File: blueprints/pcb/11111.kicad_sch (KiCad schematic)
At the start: 128 parts, among them J1 TRRS_MJ-4PP-9, J2 TRRS_MJ-4PP-9, SW1 SW_Push, SW10 SW_Push, SW11 SW_Push, SW12 SW_Push, SW13 SW_Push, SW14 SW_Push, SW15 SW_Push, SW16 SW_Push, SW17 SW_Push, SW18 SW_Push, SW19 SW_Push, SW2 SW_Push, SW20 SW_Push, SW21 SW_Push, SW22 SW_Push, SW23 SW_Push, SW24 SW_Push, SW25 SW_Push, SW26 SW_Push, SW27 SW_Push, SW28 SW_Push, SW29 SW_Push, SW3 SW_Push, SW30 SW_Push, SW31 SW_Push, SW32 SW_Push, SW33 SW_Push, SW34 SW_Push, SW35 SW_Push, SW36 SW_Push, SW37 SW_Push, SW38 SW_Push, SW39 SW_Push, SW4 SW_Push, SW40 SW_Push, SW41 SW_Push, SW42 SW_Push, SW43 SW_Push, SW44 SW_Push, SW45 SW_Push, SW46 SW_Push, SW47 SW_Push, SW48 SW_Push, SW49 SW_Push, SW5 SW_Push, SW50 SW_Push, SW51 SW_Push, SW52 SW_Push, SW53 SW_Push, SW54 SW_Push, SW55 SW_Push, SW56 SW_Push, SW57 SW_Push, SW58 SW_Push, SW59 SW_Push, SW6 SW_Push, SW60 SW_Push, SW61 SW_Push, SW62 SW_Push, SW7 SW_Push, SW8 SW_Push, SW9 SW_Push, U1 Pico, U2 Pico

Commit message: オモテウラを間違えていたので修正
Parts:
- D1, D10, D11, D12, D13, D14, D15, D16, D17, D18, D19, D2, D20, D21, D22, D23, D24, D25, D26, D27, D28, D29, D3, D30, D31, D32, D33, D34, D35, D36, D37, D38, D39, D4, D40, D41, D42, D43, D44, D45, D46, D47, D48, D49, D5, D50, D51, D52, D53, D54, D55, D56, D57, D58, D59, D6, D60, D61, D62, D7, D8, D9: footprint Diode_SMD:D_SOD-123 -> Salicylic-acid3_kbd_Parts:Diode_SMD
- SW1, SW10, SW11, SW12, SW13, SW14, SW15, SW16, SW17, SW18, SW19, SW2, SW20, SW21, SW22, SW23, SW24, SW25, SW26, SW27, SW28, SW29, SW3, SW30, SW31, SW32, SW33, SW34, SW35, SW36, SW37, SW38, SW39, SW4, SW40, SW41, SW42, SW43, SW44, SW45, SW46, SW47, SW48, SW49, SW5, SW50, SW51, SW52, SW53, SW54, SW55, SW56, SW57, SW58, SW59, SW6, SW60, SW61, SW62, SW7, SW8, SW9: footprint Button_Switch_Keyboard:SW_Cherry_MX_1.00u_PCB -> Salicylic-acid3_kbd_SW:CherryMX_Solder_1u

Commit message: update PCB
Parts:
- removed U1, U2: Pico, Raspberry-pi-pico:RPi_Pico_SMD_TH, symbol raspberry_pi_pico:Pico
- added R1, R2: 5.1k, Resistor_THT:R_Axial_DIN0204_L3.6mm_D1.6mm_P5.08mm_Vertical, symbol Device:R_Small
- added U1, U2: Pico, Raspberry-pi-pico:RPi_Pico_SMD_TH, symbol raspberry-pi-pico:Pico
- added U3: ~, keyboard_parts:USB_type-C_dip_module_AE-USB2.0-TYPE-C, symbol usb_type-c_dip_connector:USB_type-C_DIP_connector
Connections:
- net Col0: now also U1.29 (GPIO22)
- net Col1: now also U1.27 (GPIO21)
- net Col10: now also U2.25 (GPIO19)
- net Col11: now also U2.24 (GPIO18)
- net Col12: now also U2.22 (GPIO17)
- net Col13: now also U2.21 (GPIO16)
- net Col2: now also U1.26 (GPIO20)
- net Col3: now also U1.25 (GPIO19)
- net Col4: now also U1.24 (GPIO18)
- net Col5: now also U1.22 (GPIO17)
- net Col6: now also U1.21 (GPIO16)
- net Col7: now also U2.29 (GPIO22)
- net Col8: now also U2.27 (GPIO21)
- net Col9: now also U2.26 (GPIO20)
- net DataLeft: now also U1.1 (GPIO0)
- net DataRight: now also U2.1 (GPIO0)
- net GND: now also R1.2, R2.2, U1.13 (GND), U1.18 (GND), U1.23 (GND), U1.28 (GND), U1.3 (GND), U1.38 (GND), U1.8 (GND), U3.4 (GND)
- net GNDA: now also U2.13 (GND), U2.18 (GND), U2.23 (GND), U2.28 (GND), U2.3 (GND), U2.31 (GPIO26_ADC0), U2.38 (GND), U2.8 (GND)
- net Row0: now also U1.15 (GPIO11)
- net Row1: now also U1.16 (GPIO12)
- net Row2: now also U1.17 (GPIO13)
- net Row3: now also U1.19 (GPIO14)
- net Row4: now also U1.20 (GPIO15)
- net Row5: now also U2.15 (GPIO11)
- net Row6: now also U2.16 (GPIO12)
- net Row7: now also U2.17 (GPIO13)
- net Row8: now also U2.19 (GPIO14)
- net Row9: now also U2.20 (GPIO15)
- net VCC: now also U1.31 (GPIO26_ADC0), U1.39 (VSYS)
- net VDD: now also U2.39 (VSYS)
- new net CC1: R1.1, U3.5 (CC1)
- new net CC2: R2.1, U3.6 (CC2)
- new net DM: U3.2 (D-)
- new net DP: U3.3 (D+)
- no-connect marks 38 -> 45

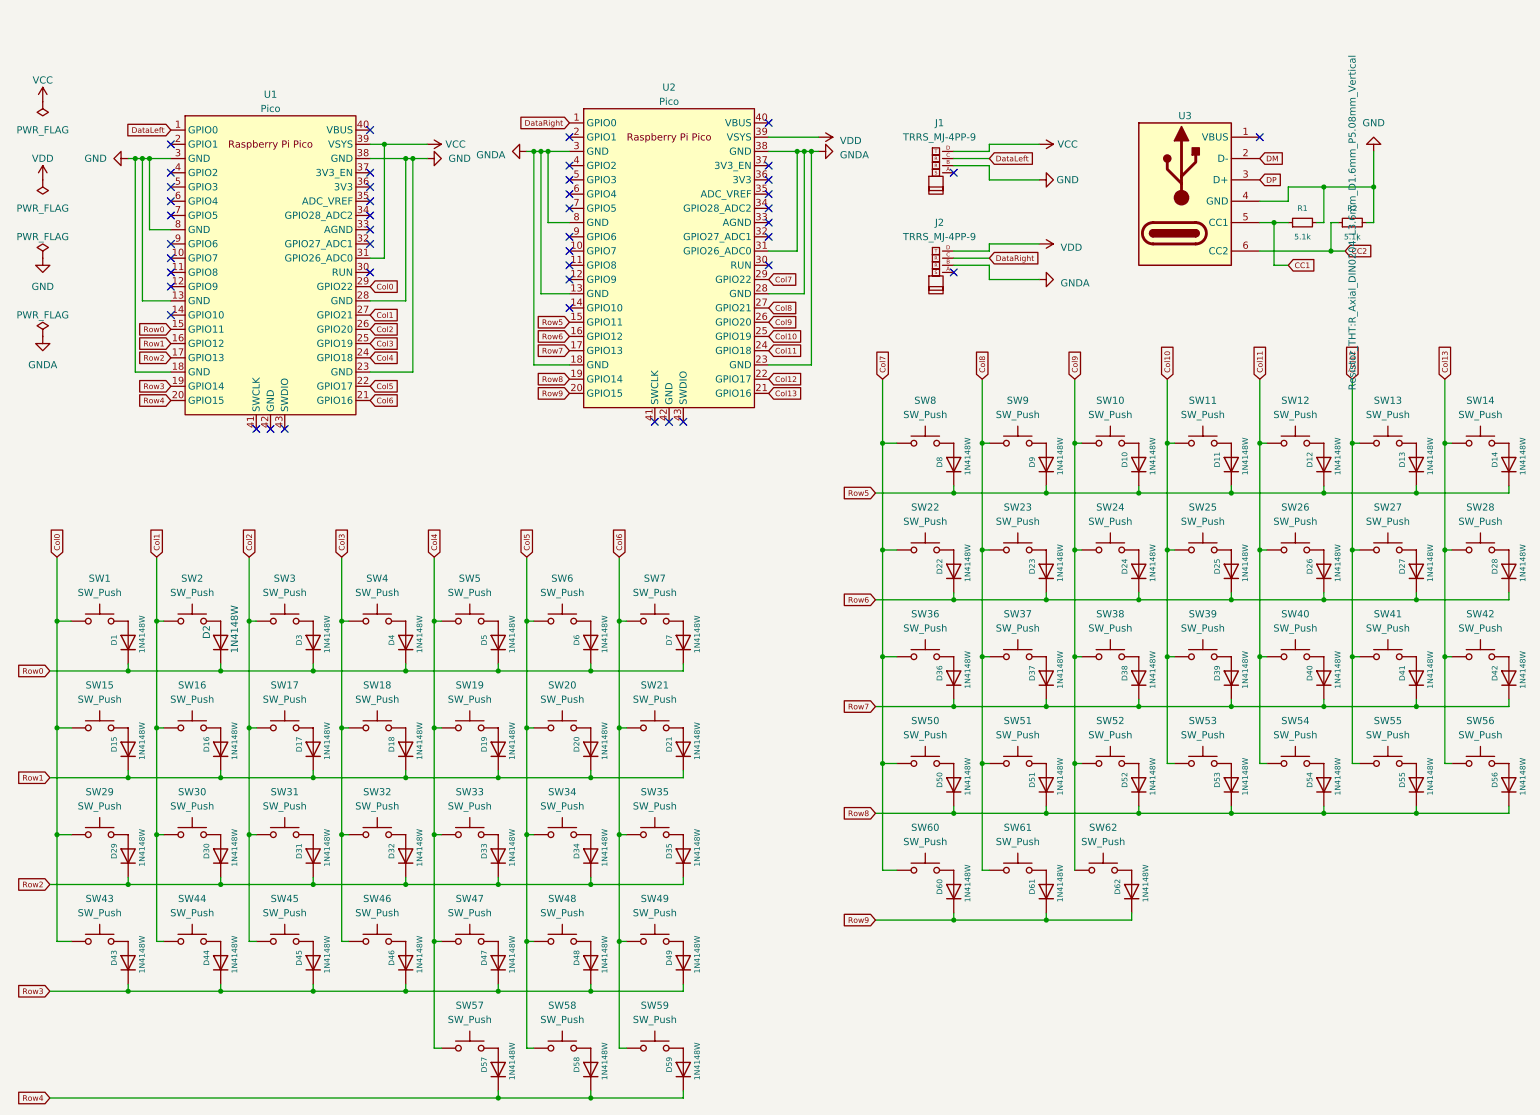
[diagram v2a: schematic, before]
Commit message: add 2 switches
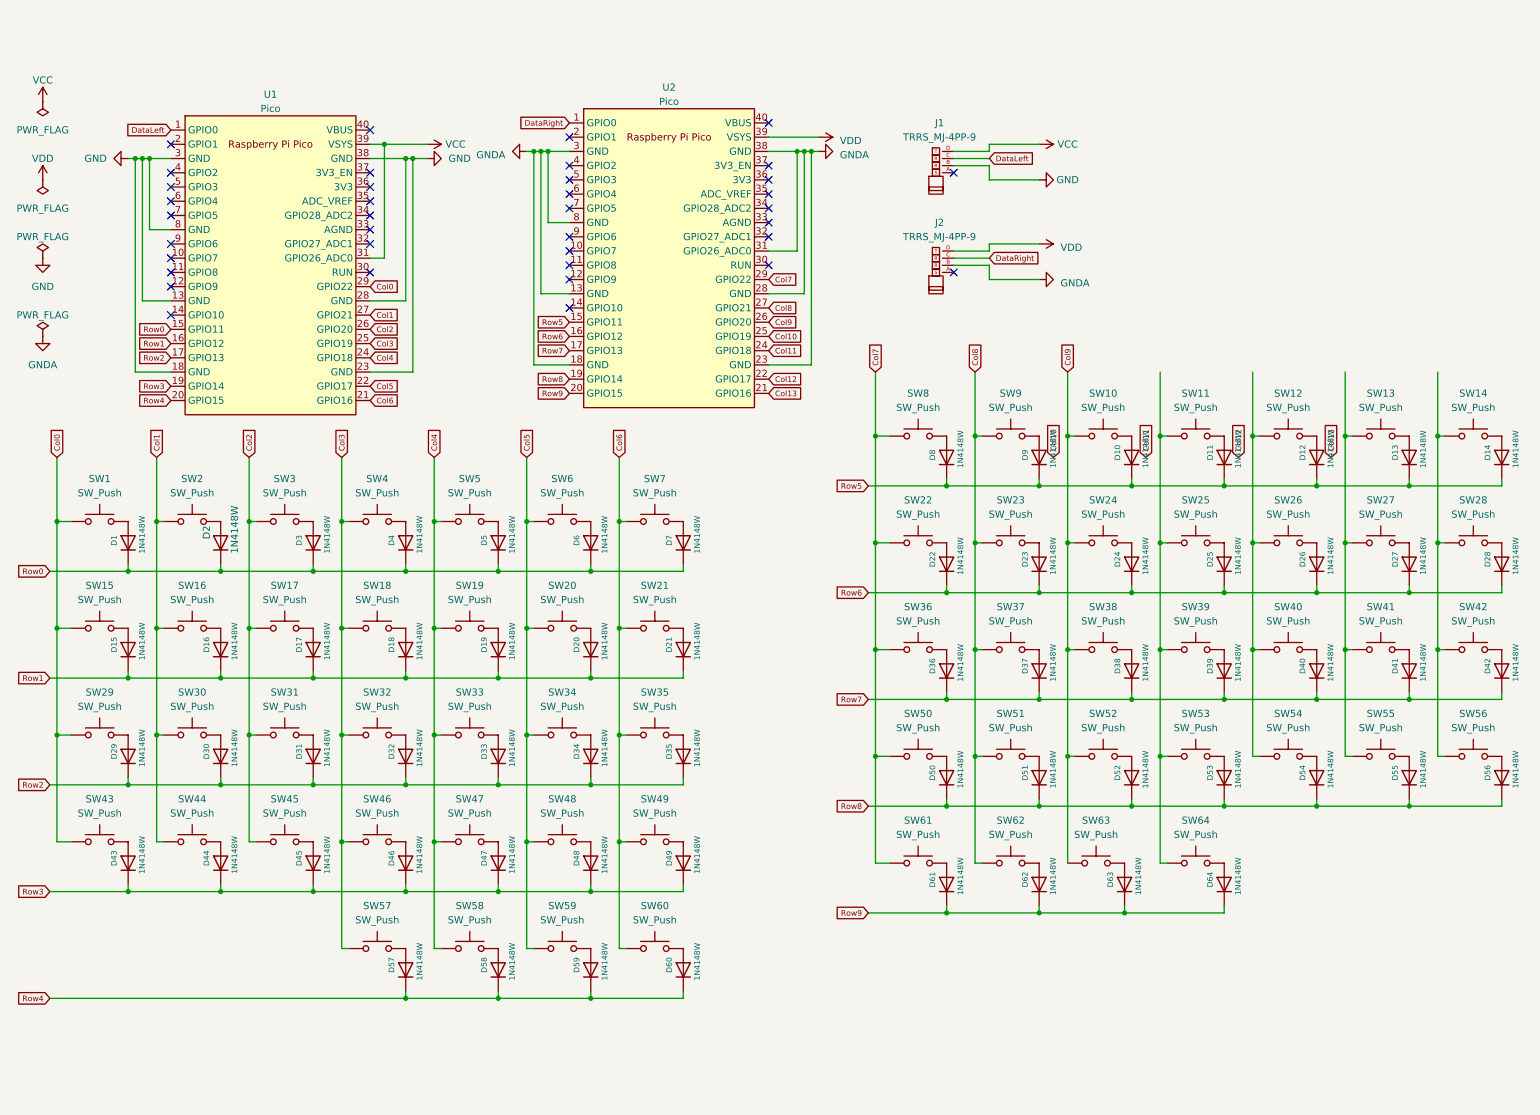
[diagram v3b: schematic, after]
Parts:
- removed R1, R2: 5.1k, Resistor_THT:R_Axial_DIN0204_L3.6mm_D1.6mm_P5.08mm_Vertical, symbol Device:R_Small
- removed U3: ~, keyboard_parts:USB_type-C_dip_module_AE-USB2.0-TYPE-C, symbol usb_type-c_dip_connector:USB_type-C_DIP_connector
- added D57, D64: 1N4148W, Salicylic-acid3_kbd_Parts:Diode_SMD, symbol Diode:1N4148W
- added SW57, SW64: SW_Push, Salicylic-acid3_kbd_SW:CherryMX_Solder_1u, symbol Switch:SW_Push
- renumbered D57 to D58, D58 to D59, D59 to D60, D60 to D61, D61 to D62, D62 to D63, SW57 to SW58, SW58 to SW59, SW59 to SW60, SW60 to SW61, SW61 to SW62, SW62 to SW63
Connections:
- net Col10: no longer SW11.1, SW25.1, SW39.1, SW53.1
- net Col11: no longer SW12.1, SW26.1, SW40.1, SW54.1
- net Col12: no longer SW13.1, SW27.1, SW41.1, SW55.1
- net Col13: no longer SW14.1, SW28.1, SW42.1, SW56.1
- net Col3: now also SW57.1
- net Row4: now also D57.1 (K)
- net Row9: now also D64.1 (K)
- new net: SW13.1, SW27.1, SW41.1, SW55.1
- new net: SW12.1, SW26.1, SW40.1, SW54.1
- new net: SW14.1, SW28.1, SW42.1, SW56.1
- new net: D64.2 (A), SW64.2
- new net: SW11.1, SW25.1, SW39.1, SW53.1, SW64.1
- new net: D57.2 (A), SW57.2
- no-connect marks 45 -> 38
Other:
- moved on the sheet: D1, D10, D11, D12, D13, D14, D15, D16, D17, D18, D19, D2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

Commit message: GNDを塗りつぶし
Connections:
- net Col10: now also SW11.1, SW25.1, SW39.1, SW53.1, SW64.1
- net Col11: now also SW12.1, SW26.1, SW40.1, SW54.1
- net Col12: now also SW13.1, SW27.1, SW41.1, SW55.1
- net Col13: now also SW14.1, SW28.1, SW42.1, SW56.1
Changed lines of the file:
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@@
     )
   )
-  (global_label "Col11" (shape input) (at 214.63 81.28 90) (fields_autoplaced)
-    (effects (font (size 1 1)) (justify left))
-    (property "Intersheetrefs" "${INTERSHEET_REFS}" (at 214.5675 75.0467 90)
+  (global_label "Col11" (shape input) (at 233.68 66.04 90) (fields_autoplaced)
+    (effects (font (size 1 1)) (justify left))
+    (property "Intersheetrefs" "${INTERSHEET_REFS}" (at 233.6175 59.8067 90)
       (effects (font (size 1 1)) (justify left) hide)
     )
@@
     )
   )
-  (global_label "Col10" (shape input) (at 198.12 81.28 90) (fields_autoplaced)
-    (effects (font (size 1 1)) (justify left))
-    (property "Intersheetrefs" "${INTERSHEET_REFS}" (at 198.0575 75.0467 90)
+  (global_label "Col10" (shape input) (at 217.17 66.04 90) (fields_autoplaced)
+    (effects (font (size 1 1)) (justify left))
+    (property "Intersheetrefs" "${INTERSHEET_REFS}" (at 217.1075 59.8067 90)
       (effects (font (size 1 1)) (justify left) hide)
     )
@@
     )
   )
+  (global_label "Col13" (shape input) (at 266.7 66.04 90) (fields_autoplaced)
+    (effects (font (size 1 1)) (justify left))
+    (property "Intersheetrefs" "${INTERSHEET_REFS}" (at 266.7 59.4187 90)
+      (effects (font (size 1 1)) (justify left) hide)
+    )
+  )
   (global_label "Row8" (shape input) (at 111.76 67.31 180) (fields_autoplaced)
     (effects (font (size 1 1)) (justify right))
@@
     )
   )
+  (global_label "Col12" (shape input) (at 250.19 66.04 90) (fields_autoplaced)
+    (effects (font (size 1 1)) (justify left))
+    (property "Intersheetrefs" "${INTERSHEET_REFS}" (at 250.19 59.4187 90)
+      (effects (font (size 1 1)) (justify left) hide)
+    )
+  )
   (global_label "Col3" (shape input) (at 71.12 81.28 90) (fields_autoplaced)
     (effects (font (size 1 1)) (justify left))
@@
     )
   )
-  (global_label "Col12" (shape input) (at 231.14 81.28 90) (fields_autoplaced)
-    (effects (font (size 1 1)) (justify left))
-    (property "Intersheetrefs" "${INTERSHEET_REFS}" (at 231.0775 75.0467 90)
-      (effects (font (size 1 1)) (justify left) hide)
-    )
-  )
   (global_label "Col2" (shape input) (at 54.61 81.28 90) (fields_autoplaced)
     (effects (font (size 1 1)) (justify left))
@@
     )
   )
-  (global_label "Col13" (shape input) (at 247.65 81.28 90) (fields_autoplaced)
-    (effects (font (size 1 1)) (justify left))
-    (property "Intersheetrefs" "${INTERSHEET_REFS}" (at 247.5875 75.0467 90)
-      (effects (font (size 1 1)) (justify left) hide)
-    )
-  )
